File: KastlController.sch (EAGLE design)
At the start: 22 parts

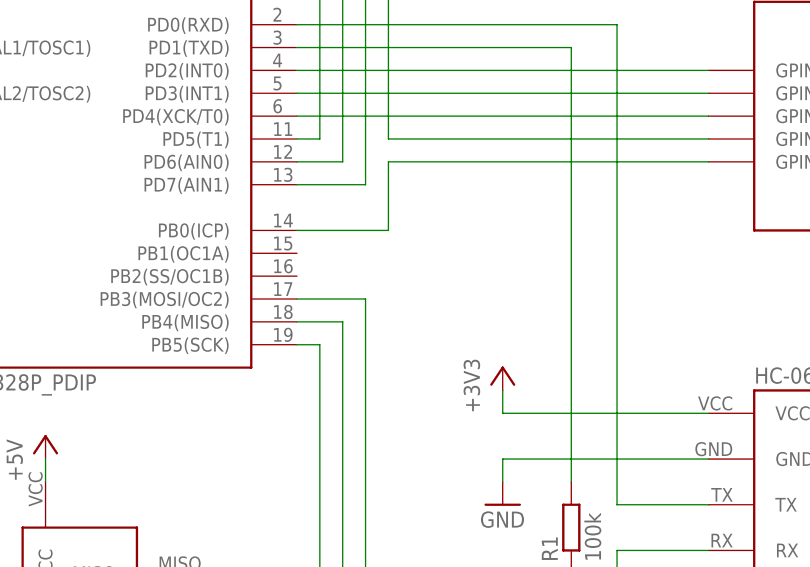
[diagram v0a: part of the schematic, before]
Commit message: Buzzer
Pin 15 is PWM Buzzer_pin
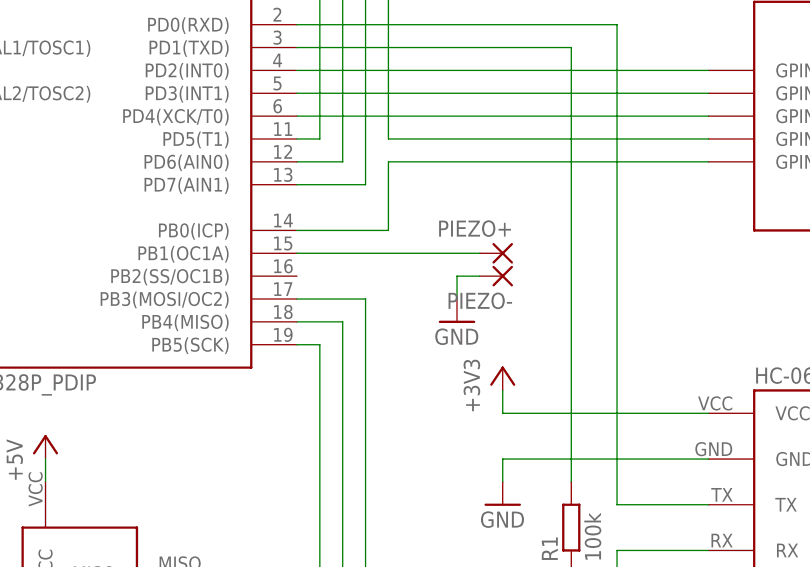
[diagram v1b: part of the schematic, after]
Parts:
- added PIEZO+, PIEZO-: (no value), wirepad:1,6/0,9
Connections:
- new net N$12: ATMEGA328P.PB1(OC1A), PIEZO+.P
- net GND: now also PIEZO-.P
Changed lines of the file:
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@@
 <part name="C2" library="htl3r-discrete" deviceset="C-EU_" device="025-024X044"/>
 <part name="GND13" library="supply1" deviceset="GND" device=""/>
+<part name="PIEZO+" library="wirepad" deviceset="1,6/0,9" device=""/>
+<part name="PIEZO-" library="wirepad" deviceset="1,6/0,9" device=""/>
+<part name="GND17" library="supply1" deviceset="GND" device=""/>
 </parts>
 <sheets>
@@
 <instance part="C2" gate="G$1" x="-20.32" y="101.6" rot="MR270"/>
 <instance part="GND13" gate="1" x="-25.4" y="88.9"/>
+<instance part="PIEZO+" gate="1" x="81.28" y="17.78" rot="MR0"/>
+<instance part="PIEZO-" gate="1" x="81.28" y="15.24" rot="R180"/>
+<instance part="GND17" gate="1" x="76.2" y="10.16"/>
 </instances>
 <busses>
@@
 <junction x="-25.4" y="101.6"/>
 <pinref part="GND13" gate="1" pin="GND"/>
+</segment>
+<segment>
+<pinref part="PIEZO-" gate="1" pin="P"/>
+<pinref part="GND17" gate="1" pin="GND"/>
+<wire x1="78.74" y1="15.24" x2="76.2" y2="15.24" width="0.1524" layer="91"/>
+<wire x1="76.2" y1="15.24" x2="76.2" y2="12.7" width="0.1524" layer="91"/>
 </segment>
 </net>
@@
 </segment>
 </net>
+<net name="N$12" class="0">
+<segment>
+<pinref part="PIEZO+" gate="1" pin="P"/>
+<pinref part="ATMEGA328P" gate="G$1" pin="PB1(OC1A)"/>
+<wire x1="78.74" y1="17.78" x2="58.42" y2="17.78" width="0.1524" layer="91"/>
+</segment>
+</net>
